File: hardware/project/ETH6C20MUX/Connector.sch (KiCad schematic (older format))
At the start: 3 parts, among them J501 Conn_01x06, J502 Conn_02x08_Odd_Even, J503 C64AC

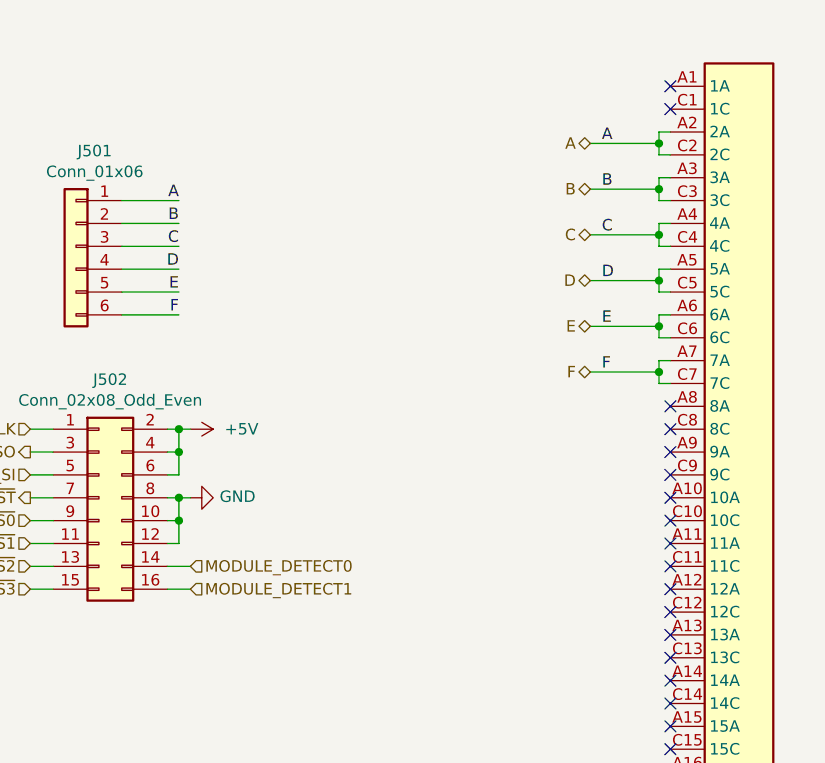
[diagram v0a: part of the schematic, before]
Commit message: Ranamed project to ETH6C20MUX. Added 4 channels. Schematic redesign and PCB layout.
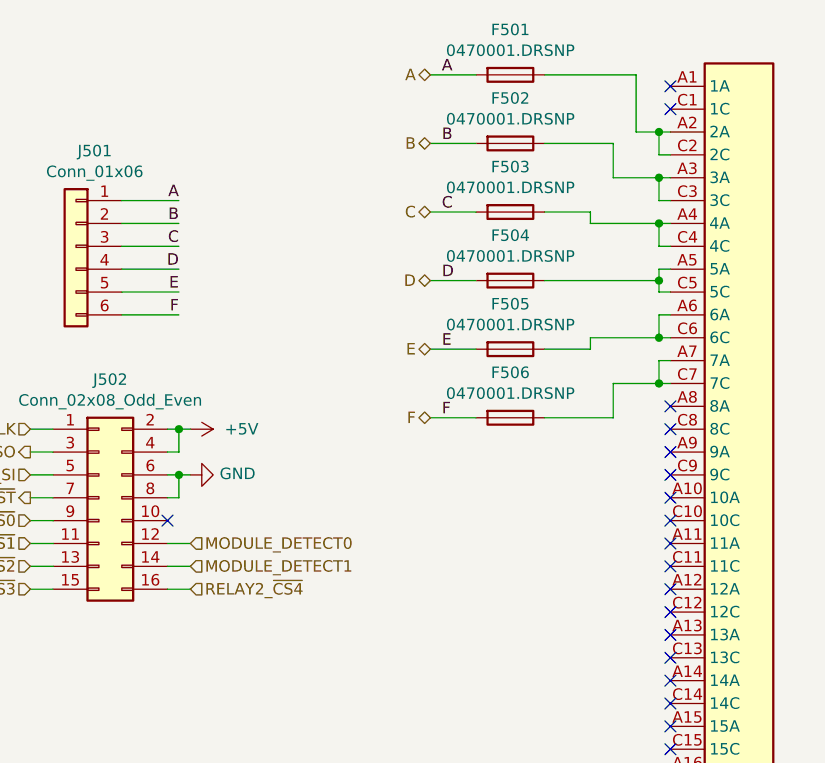
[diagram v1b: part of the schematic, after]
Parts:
- added F501, F502, F503, F504, F505, F506: 0470001.DRSNP, ETH6C16MXU:0470, symbol Device:Fuse
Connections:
- net +5V: no longer J502.6 (Pin_6)
- net A: now also F501.2; no longer J503.A2 (2A), J503.C2 (2C)
- net B: now also F502.2; no longer J503.A3 (3A), J503.C3 (3C)
- net C: now also F503.2; no longer J503.A4 (4A), J503.C4 (4C)
- net D: now also F504.2; no longer J503.A5 (5A), J503.C5 (5C)
- net E: now also F505.2; no longer J503.A6 (6A), J503.C6 (6C)
- net F: now also F506.2; no longer J503.A7 (7A), J503.C7 (7C)
- net GND: now also J502.6 (Pin_6); no longer J502.10 (Pin_10), J502.12 (Pin_12)
- net MODULE_DETECT0: now also J502.12 (Pin_12); no longer J502.14 (Pin_14)
- net MODULE_DETECT1: now also J502.14 (Pin_14); no longer J502.16 (Pin_16)
- new net: F501.1, J503.A2 (2A), J503.C2 (2C)
- new net: F502.1, J503.A3 (3A), J503.C3 (3C)
- new net: F503.1, J503.A4 (4A), J503.C4 (4C)
- new net: F504.1, J503.A5 (5A), J503.C5 (5C)
- new net: F505.1, J503.A6 (6A), J503.C6 (6C)
- new net: F506.1, J503.A7 (7A), J503.C7 (7C)
- new net RELAY2_~CS4: J502.16 (Pin_16)
- no-connect marks 36 -> 37
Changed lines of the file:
@@
 	5650 1000 5600 1000
 Wire Wire Line
-	5600 1000 5600 1050
-Wire Wire Line
 	5600 1100 5650 1100
 Wire Wire Line
 	5650 1200 5600 1200
 Wire Wire Line
-	5600 1200 5600 1250
-Wire Wire Line
 	5600 1300 5650 1300
 Wire Wire Line
 	5650 1400 5600 1400
 Wire Wire Line
-	5600 1400 5600 1450
-Wire Wire Line
 	5600 1500 5650 1500
 Wire Wire Line
 	5650 1600 5600 1600
 Wire Wire Line
-	5600 1600 5600 1650
-Wire Wire Line
 	5600 1700 5650 1700
 Wire Wire Line
 	5650 1800 5600 1800
 Wire Wire Line
-	5600 1800 5600 1850
-Wire Wire Line
 	5600 1900 5650 1900
 Wire Wire Line
 	5650 2000 5600 2000
-Wire Wire Line
-	5600 2000 5600 2050
 Wire Wire Line
 	5600 2100 5650 2100
@@
 NoConn ~ 5650 2500
 NoConn ~ 5650 2400
-Connection ~ 5600 1050
-Wire Wire Line
-	5600 1050 5600 1100
-Connection ~ 5600 1250
-Wire Wire Line
-	5600 1250 5600 1300
-Connection ~ 5600 1450
-Wire Wire Line
-	5600 1450 5600 1500
-Connection ~ 5600 1650
-Wire Wire Line
-	5600 1650 5600 1700
-Connection ~ 5600 1850
-Wire Wire Line
-	5600 1850 5600 1900
-Connection ~ 5600 2050
-Wire Wire Line
-	5600 2050 5600 2100
-Text HLabel 5300 1050 0    50   BiDi ~ 0
+Text HLabel 4600 750  0    50   BiDi ~ 0
 A
-Text HLabel 5300 1250 0    50   BiDi ~ 0
+Text HLabel 4600 1050 0    50   BiDi ~ 0
 B
-Text HLabel 5300 1450 0    50   BiDi ~ 0
+Text HLabel 4600 1350 0    50   BiDi ~ 0
 C
-Text HLabel 5300 1650 0    50   BiDi ~ 0
+Text HLabel 4600 1650 0    50   BiDi ~ 0
 D
-Text HLabel 5300 1850 0    50   BiDi ~ 0
+Text HLabel 4600 1950 0    50   BiDi ~ 0
 E
-Text HLabel 5300 2050 0    50   BiDi ~ 0
+Text HLabel 4600 2250 0    50   BiDi ~ 0
 F
 Wire Wire Line
@@
 TX-
 Wire Wire Line
-	5300 2050 5600 2050
-Wire Wire Line
-	5300 1850 5600 1850
-Wire Wire Line
-	5300 1650 5600 1650
-Wire Wire Line
-	5300 1450 5600 1450
-Wire Wire Line
-	5300 1250 5600 1250
-Wire Wire Line
-	5300 1050 5600 1050
-Text Label 5350 1050 0    50   ~ 0
+	4600 2250 4800 2250
+Wire Wire Line
+	4600 1950 4800 1950
+Wire Wire Line
+	4600 1650 4800 1650
+Wire Wire Line
+	4600 1350 4800 1350
+Wire Wire Line
+	4600 1050 4800 1050
+Wire Wire Line
+	4600 750  4800 750
+Text Label 4650 750  0    50   ~ 0
 A
-Text Label 5350 1250 0    50   ~ 0
+Text Label 4650 1050 0    50   ~ 0
 B
-Text Label 5350 1450 0    50   ~ 0
+Text Label 4650 1350 0    50   ~ 0
 C
-Text Label 5350 1650 0    50   ~ 0
+Text Label 4650 1650 0    50   ~ 0
 D
-Text Label 5350 1850 0    50   ~ 0
+Text Label 4650 1950 0    50   ~ 0
 E
-Text Label 5350 2050 0    50   ~ 0
+Text Label 4650 2250 0    50   ~ 0
 F
 Wire Wire Line
-	3550 2600 3500 2600
-Wire Wire Line
-	3450 2700 3500 2700
-Wire Wire Line
-	3500 2600 3500 2700
-Connection ~ 3500 2600
+	3550 2500 3500 2500
 Wire Wire Line
 	3450 2600 3500 2600
+Wire Wire Line
+	3500 2500 3500 2600
+Connection ~ 3500 2500
+Wire Wire Line
+	3450 2500 3500 2500
 Wire Wire Line
 	3500 2300 3550 2300
@@
 	2850 2600 2950 2600
 Wire Wire Line
-	3550 3000 3450 3000
-Wire Wire Line
 	3550 2900 3450 2900
+Wire Wire Line
+	3550 2800 3450 2800
 Wire Wire Line
 	2950 2500 2850 2500
@@
 L power:GND #PWR0502
 U 1 1 5D777B58
-P 3550 2600
+P 3550 2500
 AR Path="/5DB25E5A/5D777B58" Ref="#PWR0502"  Part="1"
 AR Path="/5D7599BA/5D777B58" Ref="#PWR?"  Part="1"
-F 0 "#PWR0502" H 3550 2350 50  0001 C CNN
-F 1 "GND" V 3555 2472 50  0000 R CNN
-F 2 "" H 3550 2600 50  0001 C CNN
-F 3 "" H 3550 2600 50  0001 C CNN
-	1    3550 2600
+F 0 "#PWR0502" H 3550 2250 50  0001 C CNN
+F 1 "GND" V 3555 2372 50  0000 R CNN
+F 2 "" H 3550 2500 50  0001 C CNN
+F 3 "" H 3550 2500 50  0001 C CNN
+	1    3550 2500
 	0    -1   -1   0
 $EndComp
@@
 Wire Wire Line
 	3250 1800 3500 1800
-Wire Wire Line
-	3500 2700 3500 2800
-Wire Wire Line
-	3500 2800 3450 2800
-Connection ~ 3500 2700
 NoConn ~ 5650 2200
 NoConn ~ 5650 2300
@@
 Text HLabel 2850 2600 0    50   Output ~ 0
 RELAY2_~RST
+Text HLabel 3550 2800 2    50   Input ~ 0
+MODULE_DETECT0
 Text HLabel 3550 2900 2    50   Input ~ 0
-MODULE_DETECT0
-Text HLabel 3550 3000 2    50   Input ~ 0
 MODULE_DETECT1
 Text HLabel 2850 3000 0    50   Input ~ 0
@@
 Wire Wire Line
 	2850 3000 2950 3000
-Wire Wire Line
-	3450 2500 3500 2500
-Wire Wire Line
-	3500 2500 3500 2400
-Connection ~ 3500 2400
 $Comp
 L Connector_Generic:Conn_02x08_Odd_Even J502
@@
 	1    0    0    -1
 $EndComp
+Wire Wire Line
+	5600 1000 5600 1100
+Wire Wire Line
+	5600 1200 5600 1300
+Wire Wire Line
+	5600 1400 5600 1500
+Wire Wire Line
+	5600 1600 5600 1650
+Wire Wire Line
+	5600 1800 5600 1900
+Wire Wire Line
+	5600 2000 5600 2100
+$Comp
+L Device:Fuse F501
+U 1 1 5D85BE06
+P 4950 750
+F 0 "F501" V 4753 750 50  0000 C CNN
+F 1 "0470001.DRSNP" V 4844 750 50  0000 C CNN
+F 2 "ETH6C16MXU:0470" V 4880 750 50  0001 C CNN
+F 3 "~" H 4950 750 50  0001 C CNN
+	1    4950 750
+	0    1    1    0
+$EndComp
+$Comp
+L Device:Fuse F502
+U 1 1 5D86B547
+P 4950 1050
+F 0 "F502" V 4753 1050 50  0000 C CNN
+F 1 "0470001.DRSNP" V 4844 1050 50  0000 C CNN
+F 2 "ETH6C16MXU:0470" V 4880 1050 50  0001 C CNN
+F 3 "~" H 4950 1050 50  0001 C CNN
+	1    4950 1050
+	0    1    1    0
+$EndComp
+$Comp
+L Device:Fuse F503
+U 1 1 5D873848
+P 4950 1350
+F 0 "F503" V 4753 1350 50  0000 C CNN
+F 1 "0470001.DRSNP" V 4844 1350 50  0000 C CNN
+F 2 "ETH6C16MXU:0470" V 4880 1350 50  0001 C CNN
+F 3 "~" H 4950 1350 50  0001 C CNN
+	1    4950 1350
+	0    1    1    0
+$EndComp
+$Comp
+L Device:Fuse F504
+U 1 1 5D878920
+P 4950 1650
+F 0 "F504" V 4753 1650 50  0000 C CNN
+F 1 "0470001.DRSNP" V 4844 1650 50  0000 C CNN
+F 2 "ETH6C16MXU:0470" V 4880 1650 50  0001 C CNN
+F 3 "~" H 4950 1650 50  0001 C CNN
+	1    4950 1650
+	0    1    1    0
+$EndComp
+$Comp
+L Device:Fuse F505
+U 1 1 5D87E9B8
+P 4950 1950
+F 0 "F505" V 4753 1950 50  0000 C CNN
+F 1 "0470001.DRSNP" V 4844 1950 50  0000 C CNN
+F 2 "ETH6C16MXU:0470" V 4880 1950 50  0001 C CNN
+F 3 "~" H 4950 1950 50  0001 C CNN
+	1    4950 1950
+	0    1    1    0
+$EndComp
+$Comp
+L Device:Fuse F506
+U 1 1 5D888312
+P 4950 2250
+F 0 "F506" V 4753 2250 50  0000 C CNN
+F 1 "0470001.DRSNP" V 4844 2250 50  0000 C CNN
+F 2 "ETH6C16MXU:0470" V 4880 2250 50  0001 C CNN
+F 3 "~" H 4950 2250 50  0001 C CNN
+	1    4950 2250
+	0    1    1    0
+$EndComp
+Wire Wire Line
+	5100 750  5500 750
+Wire Wire Line
+	5500 750  5500 1000
+Wire Wire Line
+	5500 1000 5600 1000
+Connection ~ 5600 1000
+Wire Wire Line
+	5100 1050 5400 1050
+Wire Wire Line
+	5400 1050 5400 1200
+Wire Wire Line
+	5400 1200 5600 1200
+Connection ~ 5600 1200
+Wire Wire Line
+	5100 1350 5300 1350
+Wire Wire Line
+	5300 1350 5300 1400
+Wire Wire Line
+	5300 1400 5600 1400
+Connection ~ 5600 1400
+Wire Wire Line
+	5600 1650 5100 1650
+Connection ~ 5600 1650
+Wire Wire Line
+	5600 1650 5600 1700
+Wire Wire Line
+	5100 1950 5300 1950
+Wire Wire Line
+	5300 1950 5300 1900
+Wire Wire Line
+	5300 1900 5600 1900
+Connection ~ 5600 1900
+Wire Wire Line
+	5100 2250 5400 2250
+Wire Wire Line
+	5400 2250 5400 2100
+Wire Wire Line
+	5400 2100 5600 2100
+Connection ~ 5600 2100
+Text HLabel 3550 3000 2    50   Input ~ 0
+RELAY2_~CS4
+Wire Wire Line
+	3550 3000 3450 3000
+NoConn ~ 3450 2700
 $EndSCHEMATC
